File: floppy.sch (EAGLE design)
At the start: 20 parts, among them IC1 ATTINY13-20SU, Q1 S9018

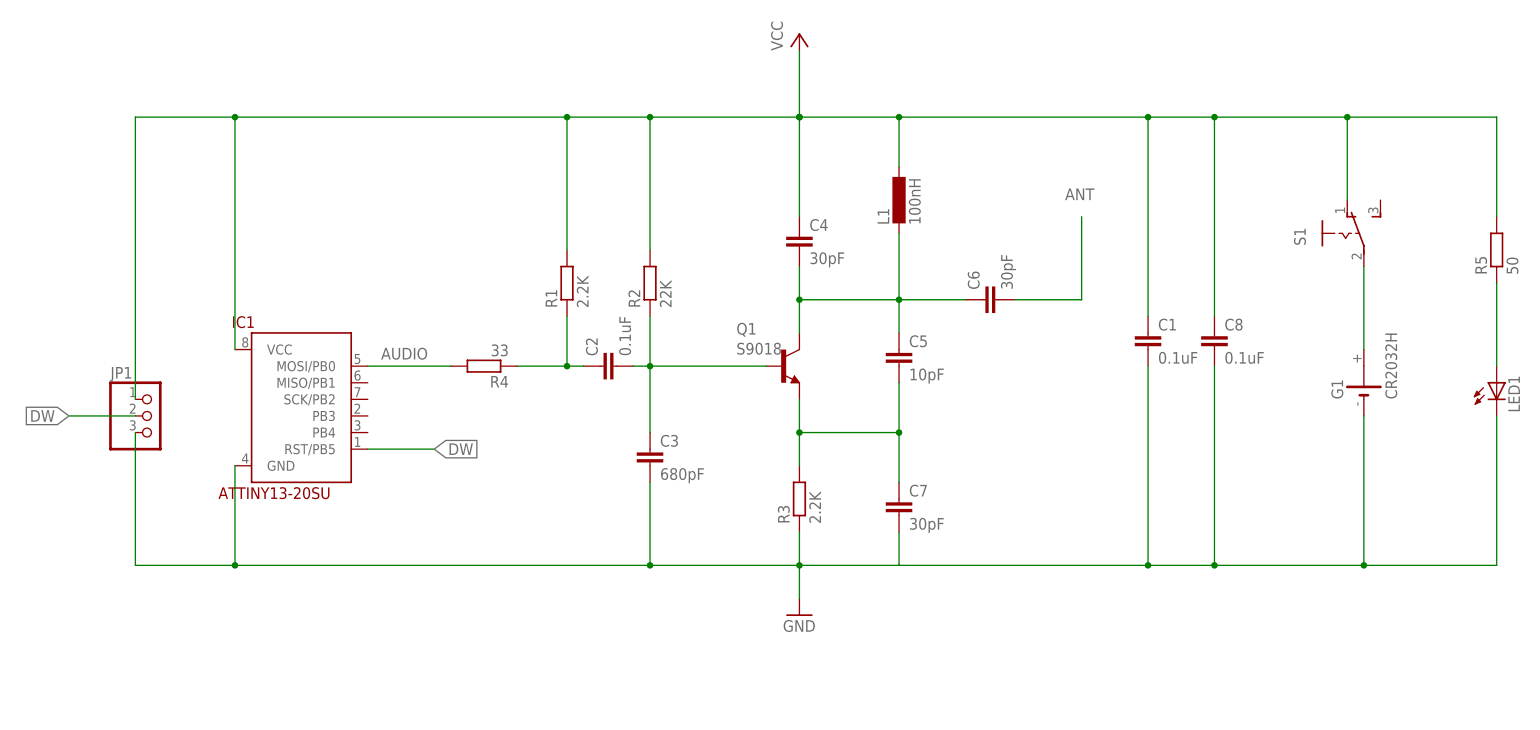
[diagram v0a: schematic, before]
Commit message: Made layout much nicer LED now driven directly from AVR TODO: * check that LED can be driven driectly from AVR * pirate flag and nicer "illegal radio transmitter" text * adjust FM frequency text * check that design works in general
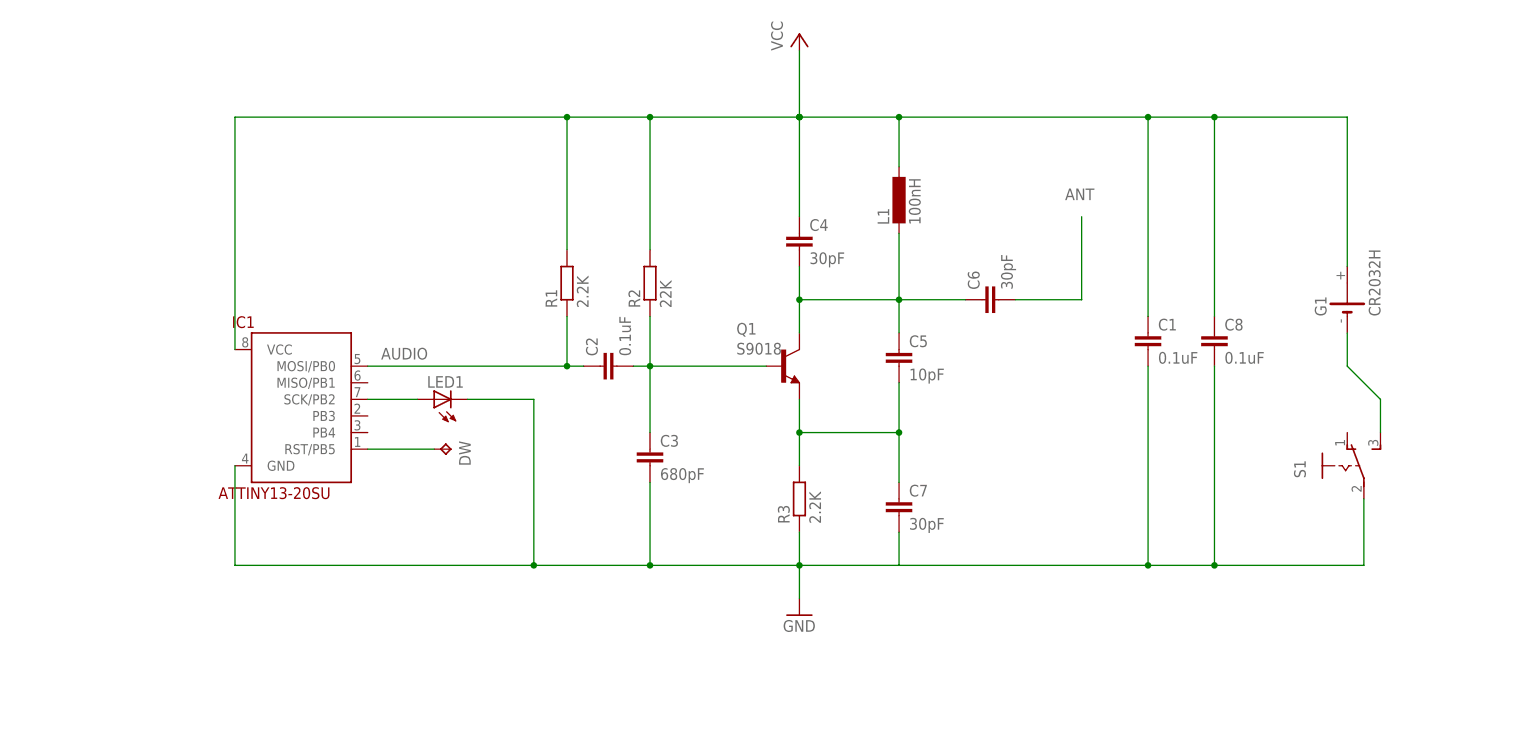
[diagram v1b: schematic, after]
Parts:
- removed JP1: (no value), pinhead:PINHD-1X3
- removed R4: 33, rcl:R-EU_0207/7
- removed R5: 50, rcl:R-EU_0207/7
- added DW: TPB1,27, testpad:TPB1,27
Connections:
- removed net N$9: LED1.A, R5.1
- net AUDIO: now also C2.1, R1.1; no longer R4.2
- net DW: now also DW.TP; no longer JP1.2
- net GND: now also S1.P; no longer G1.-, JP1.3
- net N$3: now also G1.-, S1.S; no longer G1.+, S1.P
- net N$5: now also IC1.SCK/PB2, LED1.A; no longer C2.1, R1.1, R4.1
- net VCC: now also G1.+; no longer JP1.1, R5.2, S1.O
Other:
- moved on the sheet: G1, LED1, S1
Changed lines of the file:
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@@
 <part name="R2" library="rcl" deviceset="R-EU_" device="0207/7" value="22K"/>
 <part name="R3" library="rcl" deviceset="R-EU_" device="0207/7" value="2.2K"/>
-<part name="R4" library="rcl" deviceset="R-EU_" device="0207/7" value="33"/>
 <part name="C1" library="rcl" deviceset="C-EU" device="025-025X050" value="0.1uF"/>
 <part name="C2" library="rcl" deviceset="C-EU" device="025-025X050" value="0.1uF"/>
@@
 <part name="P+1" library="supply1" deviceset="VCC" device=""/>
 <part name="GND1" library="supply1" deviceset="GND" device=""/>
-<part name="R5" library="rcl" deviceset="R-EU_" device="0207/7" value="50"/>
 <part name="LED1" library="led" deviceset="LED" device="5MM"/>
 <part name="IC1" library="attiny13" deviceset="ATTINY13-20*" device="SU"/>
-<part name="JP1" library="pinhead" deviceset="PINHD-1X3" device=""/>
+<part name="DW" library="testpad" deviceset="TP" device="B1,27"/>
 </parts>
 <sheets>
@@
 <instance part="R2" gate="G$1" x="58.42" y="81.28" rot="R90"/>
 <instance part="R3" gate="G$1" x="81.28" y="48.26" rot="R90"/>
-<instance part="R4" gate="G$1" x="33.02" y="68.58" rot="R180"/>
 <instance part="C1" gate="G$1" x="134.62" y="73.66"/>
 <instance part="C2" gate="G$1" x="50.8" y="68.58" rot="R90"/>
@@
 </instance>
 <instance part="L1" gate="G$1" x="96.52" y="93.98"/>
-<instance part="S1" gate="1" x="165.1" y="88.9"/>
-<instance part="G1" gate="1" x="167.64" y="66.04" rot="R90"/>
+<instance part="S1" gate="1" x="165.1" y="53.34"/>
+<instance part="G1" gate="1" x="165.1" y="78.74" rot="R90"/>
 <instance part="P+1" gate="VCC" x="81.28" y="119.38"/>
 <instance part="GND1" gate="1" x="81.28" y="30.48"/>
-<instance part="R5" gate="G$1" x="187.96" y="86.36" rot="R90"/>
-<instance part="LED1" gate="G$1" x="187.96" y="66.04"/>
+<instance part="LED1" gate="G$1" x="25.4" y="63.5" rot="R90"/>
 <instance part="IC1" gate="G$1" x="5.08" y="63.5"/>
-<instance part="JP1" gate="A" x="-17.78" y="60.96"/>
+<instance part="DW" gate="G$1" x="27.94" y="55.88" rot="R270"/>
 </instances>
 <busses>
 </busses>
 <nets>
-<net name="N$3" class="0">
-<segment>
-<pinref part="S1" gate="1" pin="P"/>
-<pinref part="G1" gate="1" pin="+"/>
-<wire x1="167.64" y1="71.12" x2="167.64" y2="83.82" width="0.1524" layer="91"/>
-</segment>
-</net>
 <net name="GND" class="0">
 <segment>
@@
 <pinref part="GND1" gate="1" pin="GND"/>
 <wire x1="81.28" y1="33.02" x2="81.28" y2="38.1" width="0.1524" layer="91"/>
-<pinref part="G1" gate="1" pin="-"/>
 <wire x1="81.28" y1="38.1" x2="81.28" y2="43.18" width="0.1524" layer="91"/>
 <wire x1="58.42" y1="38.1" x2="81.28" y2="38.1" width="0.1524" layer="91"/>
@@
 <wire x1="134.62" y1="38.1" x2="144.78" y2="38.1" width="0.1524" layer="91"/>
 <wire x1="144.78" y1="38.1" x2="167.64" y2="38.1" width="0.1524" layer="91"/>
-<wire x1="167.64" y1="38.1" x2="167.64" y2="60.96" width="0.1524" layer="91"/>
 <pinref part="C3" gate="G$1" pin="2"/>
 <wire x1="58.42" y1="50.8" x2="58.42" y2="38.1" width="0.1524" layer="91"/>
@@
 <wire x1="144.78" y1="68.58" x2="144.78" y2="38.1" width="0.1524" layer="91"/>
 <junction x="144.78" y="38.1"/>
-<wire x1="167.64" y1="38.1" x2="187.96" y2="38.1" width="0.1524" layer="91"/>
-<wire x1="187.96" y1="38.1" x2="187.96" y2="60.96" width="0.1524" layer="91"/>
-<pinref part="LED1" gate="G$1" pin="C"/>
-<junction x="167.64" y="38.1"/>
 <pinref part="C1" gate="G$1" pin="2"/>
 <wire x1="134.62" y1="68.58" x2="134.62" y2="38.1" width="0.1524" layer="91"/>
 <junction x="134.62" y="38.1"/>
-<wire x1="58.42" y1="38.1" x2="-5.08" y2="38.1" width="0.1524" layer="91"/>
+<wire x1="58.42" y1="38.1" x2="40.64" y2="38.1" width="0.1524" layer="91"/>
 <pinref part="IC1" gate="G$1" pin="GND"/>
-<wire x1="-5.08" y1="38.1" x2="-20.32" y2="38.1" width="0.1524" layer="91"/>
+<wire x1="40.64" y1="38.1" x2="-5.08" y2="38.1" width="0.1524" layer="91"/>
 <wire x1="-5.08" y1="53.34" x2="-5.08" y2="38.1" width="0.1524" layer="91"/>
-<junction x="-5.08" y="38.1"/>
-<pinref part="JP1" gate="A" pin="3"/>
-<wire x1="-20.32" y1="38.1" x2="-20.32" y2="58.42" width="0.1524" layer="91"/>
 <junction x="58.42" y="38.1"/>
 <junction x="81.28" y="38.1"/>
+<pinref part="LED1" gate="G$1" pin="C"/>
+<wire x1="30.48" y1="63.5" x2="40.64" y2="63.5" width="0.1524" layer="91"/>
+<wire x1="40.64" y1="63.5" x2="40.64" y2="38.1" width="0.1524" layer="91"/>
+<junction x="40.64" y="38.1"/>
+<pinref part="S1" gate="1" pin="P"/>
+<wire x1="167.64" y1="38.1" x2="167.64" y2="48.26" width="0.1524" layer="91"/>
 </segment>
 </net>
 <net name="VCC" class="0">
 <segment>
-<pinref part="S1" gate="1" pin="O"/>
-<wire x1="165.1" y1="93.98" x2="165.1" y2="106.68" width="0.1524" layer="91"/>
 <wire x1="165.1" y1="106.68" x2="144.78" y2="106.68" width="0.1524" layer="91"/>
 <wire x1="144.78" y1="106.68" x2="134.62" y2="106.68" width="0.1524" layer="91"/>
@@
 <wire x1="144.78" y1="76.2" x2="144.78" y2="106.68" width="0.1524" layer="91"/>
 <junction x="144.78" y="106.68"/>
-<wire x1="165.1" y1="106.68" x2="187.96" y2="106.68" width="0.1524" layer="91"/>
-<wire x1="187.96" y1="106.68" x2="187.96" y2="91.44" width="0.1524" layer="91"/>
-<pinref part="R5" gate="G$1" pin="2"/>
-<junction x="165.1" y="106.68"/>
 <pinref part="C1" gate="G$1" pin="1"/>
 <wire x1="134.62" y1="106.68" x2="134.62" y2="76.2" width="0.1524" layer="91"/>
@@
 <wire x1="45.72" y1="106.68" x2="-5.08" y2="106.68" width="0.1524" layer="91"/>
 <pinref part="IC1" gate="G$1" pin="VCC"/>
-<wire x1="-5.08" y1="106.68" x2="-20.32" y2="106.68" width="0.1524" layer="91"/>
 <wire x1="-5.08" y1="71.12" x2="-5.08" y2="106.68" width="0.1524" layer="91"/>
-<pinref part="JP1" gate="A" pin="1"/>
-<wire x1="-20.32" y1="63.5" x2="-20.32" y2="106.68" width="0.1524" layer="91"/>
-<junction x="-5.08" y="106.68"/>
 <junction x="45.72" y="106.68"/>
+<pinref part="G1" gate="1" pin="+"/>
+<wire x1="165.1" y1="83.82" x2="165.1" y2="106.68" width="0.1524" layer="91"/>
 </segment>
 </net>
@@
 </segment>
 </net>
-<net name="N$5" class="0">
-<segment>
+<net name="ANT" class="0">
+<segment>
+<pinref part="C6" gate="G$1" pin="2"/>
+<wire x1="114.3" y1="78.74" x2="124.46" y2="78.74" width="0.1524" layer="91"/>
+<wire x1="124.46" y1="78.74" x2="124.46" y2="91.44" width="0.1524" layer="91"/>
+<label x="121.92" y="93.98" size="1.778" layer="95"/>
+</segment>
+</net>
+<net name="AUDIO" class="0">
+<segment>
+<label x="17.272" y="69.596" size="1.778" layer="95"/>
+<pinref part="IC1" gate="G$1" pin="MOSI/PB0"/>
+<wire x1="45.72" y1="68.58" x2="15.24" y2="68.58" width="0.1524" layer="91"/>
 <pinref part="R1" gate="G$1" pin="1"/>
 <pinref part="C2" gate="G$1" pin="1"/>
 <wire x1="45.72" y1="76.2" x2="45.72" y2="68.58" width="0.1524" layer="91"/>
 <wire x1="45.72" y1="68.58" x2="48.26" y2="68.58" width="0.1524" layer="91"/>
-<pinref part="R4" gate="G$1" pin="1"/>
-<wire x1="45.72" y1="68.58" x2="38.1" y2="68.58" width="0.1524" layer="91"/>
 <junction x="45.72" y="68.58"/>
-</segment>
-</net>
-<net name="ANT" class="0">
-<segment>
-<pinref part="C6" gate="G$1" pin="2"/>
-<wire x1="114.3" y1="78.74" x2="124.46" y2="78.74" width="0.1524" layer="91"/>
-<wire x1="124.46" y1="78.74" x2="124.46" y2="91.44" width="0.1524" layer="91"/>
-<label x="121.92" y="93.98" size="1.778" layer="95"/>
-</segment>
-</net>
-<net name="N$9" class="0">
-<segment>
-<pinref part="R5" gate="G$1" pin="1"/>
-<pinref part="LED1" gate="G$1" pin="A"/>
-<wire x1="187.96" y1="68.58" x2="187.96" y2="81.28" width="0.1524" layer="91"/>
-</segment>
-</net>
-<net name="AUDIO" class="0">
-<segment>
-<pinref part="R4" gate="G$1" pin="2"/>
-<label x="17.272" y="69.596" size="1.778" layer="95"/>
-<pinref part="IC1" gate="G$1" pin="MOSI/PB0"/>
-<wire x1="27.94" y1="68.58" x2="15.24" y2="68.58" width="0.1524" layer="91"/>
 </segment>
 </net>
@@
 <pinref part="IC1" gate="G$1" pin="RST/PB5"/>
 <wire x1="25.4" y1="55.88" x2="15.24" y2="55.88" width="0.1524" layer="91"/>
-<label x="25.4" y="55.88" size="1.778" layer="95" xref="yes"/>
-</segment>
-<segment>
-<pinref part="JP1" gate="A" pin="2"/>
-<wire x1="-20.32" y1="60.96" x2="-30.48" y2="60.96" width="0.1524" layer="91"/>
-<label x="-30.48" y="60.96" size="1.778" layer="95" rot="R180" xref="yes"/>
-</segment>
-</net>
+<pinref part="DW" gate="G$1" pin="TP"/>
+</segment>
+</net>
+<net name="N$5" class="0">
+<segment>
+<pinref part="IC1" gate="G$1" pin="SCK/PB2"/>
+<pinref part="LED1" gate="G$1" pin="A"/>
+<wire x1="15.24" y1="63.5" x2="22.86" y2="63.5" width="0.1524" layer="91"/>
+</segment>
+</net>
+<net name="N$3" class="0">
+<segment>
+<pinref part="S1" gate="1" pin="S"/>
+<wire x1="170.18" y1="58.42" x2="170.18" y2="63.5" width="0.1524" layer="91"/>
+<wire x1="170.18" y1="63.5" x2="165.1" y2="68.58" width="0.1524" layer="91"/>
+<pinref part="G1" gate="1" pin="-"/>
+<wire x1="165.1" y1="68.58" x2="165.1" y2="73.66" width="0.1524" layer="91"/>
+</segment>
+</net>

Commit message: Fixed battery holder footprint Added "Illegal radio transmitter"
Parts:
- G1: value CR2032H -> BK-913; device battery:CR2032H -> local:BK-913
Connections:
- net N$3: now also G1.V-; no longer G1.-
- net VCC: now also G1.V+; no longer G1.+
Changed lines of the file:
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@@
 <part name="L1" library="rcl" deviceset="L-EU" device="0207/7" value="100nH"/>
 <part name="S1" library="switch" deviceset="255SB" device=""/>
-<part name="G1" library="battery" deviceset="CR2032H" device=""/>
+<part name="G1" library="local" deviceset="BK-913" device=""/>
 <part name="P+1" library="supply1" deviceset="VCC" device=""/>
 <part name="GND1" library="supply1" deviceset="GND" device=""/>
@@
 <instance part="L1" gate="G$1" x="96.52" y="93.98"/>
 <instance part="S1" gate="1" x="165.1" y="53.34"/>
-<instance part="G1" gate="1" x="165.1" y="78.74" rot="R90"/>
+<instance part="G1" gate="G$1" x="165.1" y="78.74" rot="R90"/>
 <instance part="P+1" gate="VCC" x="81.28" y="119.38"/>
 <instance part="GND1" gate="1" x="81.28" y="30.48"/>
@@
 <wire x1="-5.08" y1="71.12" x2="-5.08" y2="106.68" width="0.1524" layer="91"/>
 <junction x="45.72" y="106.68"/>
-<pinref part="G1" gate="1" pin="+"/>
+<pinref part="G1" gate="G$1" pin="V+"/>
 <wire x1="165.1" y1="83.82" x2="165.1" y2="106.68" width="0.1524" layer="91"/>
 </segment>
@@
 <wire x1="170.18" y1="58.42" x2="170.18" y2="63.5" width="0.1524" layer="91"/>
 <wire x1="170.18" y1="63.5" x2="165.1" y2="68.58" width="0.1524" layer="91"/>
-<pinref part="G1" gate="1" pin="-"/>
+<pinref part="G1" gate="G$1" pin="V-"/>
 <wire x1="165.1" y1="68.58" x2="165.1" y2="73.66" width="0.1524" layer="91"/>
 </segment>

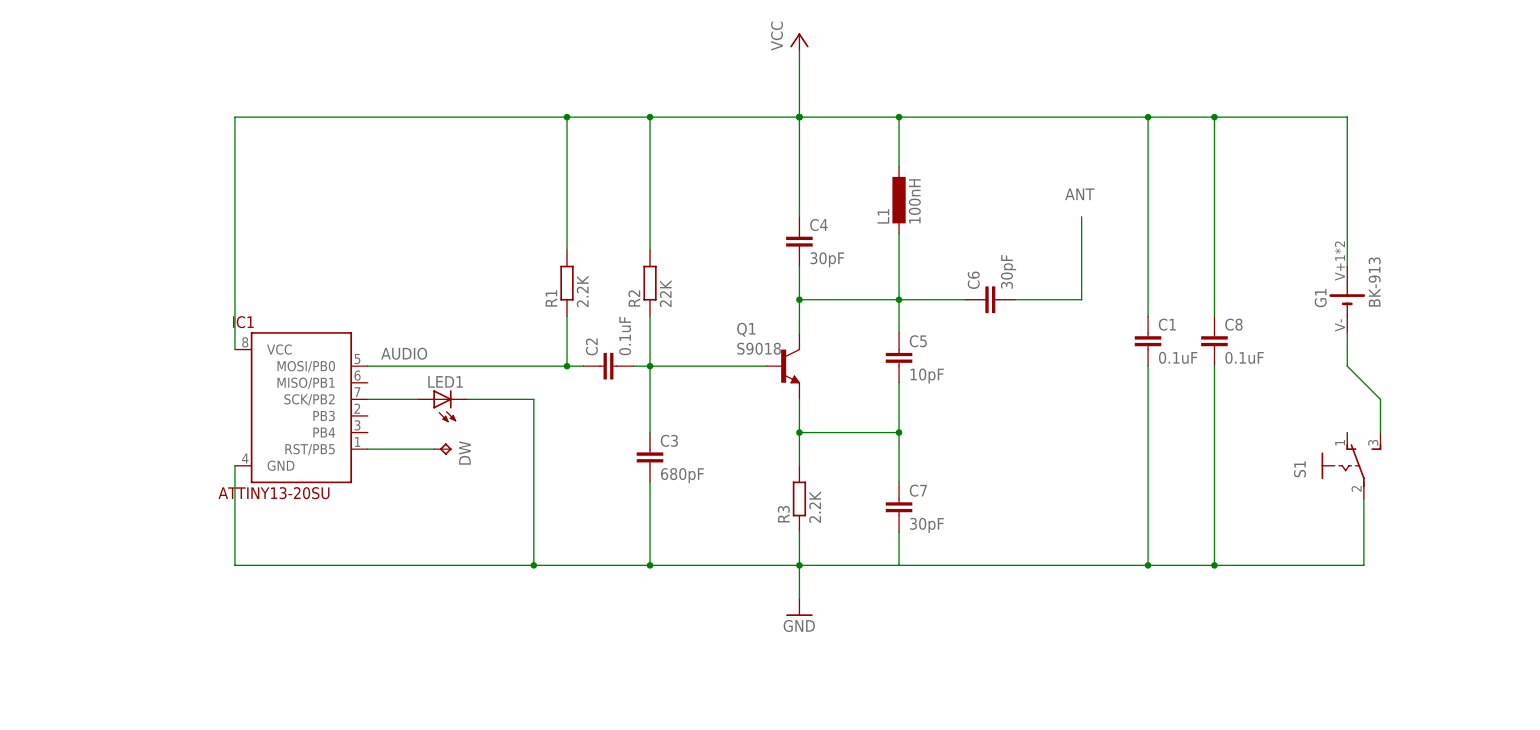
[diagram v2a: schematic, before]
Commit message: New circuit that has been tested to work up front
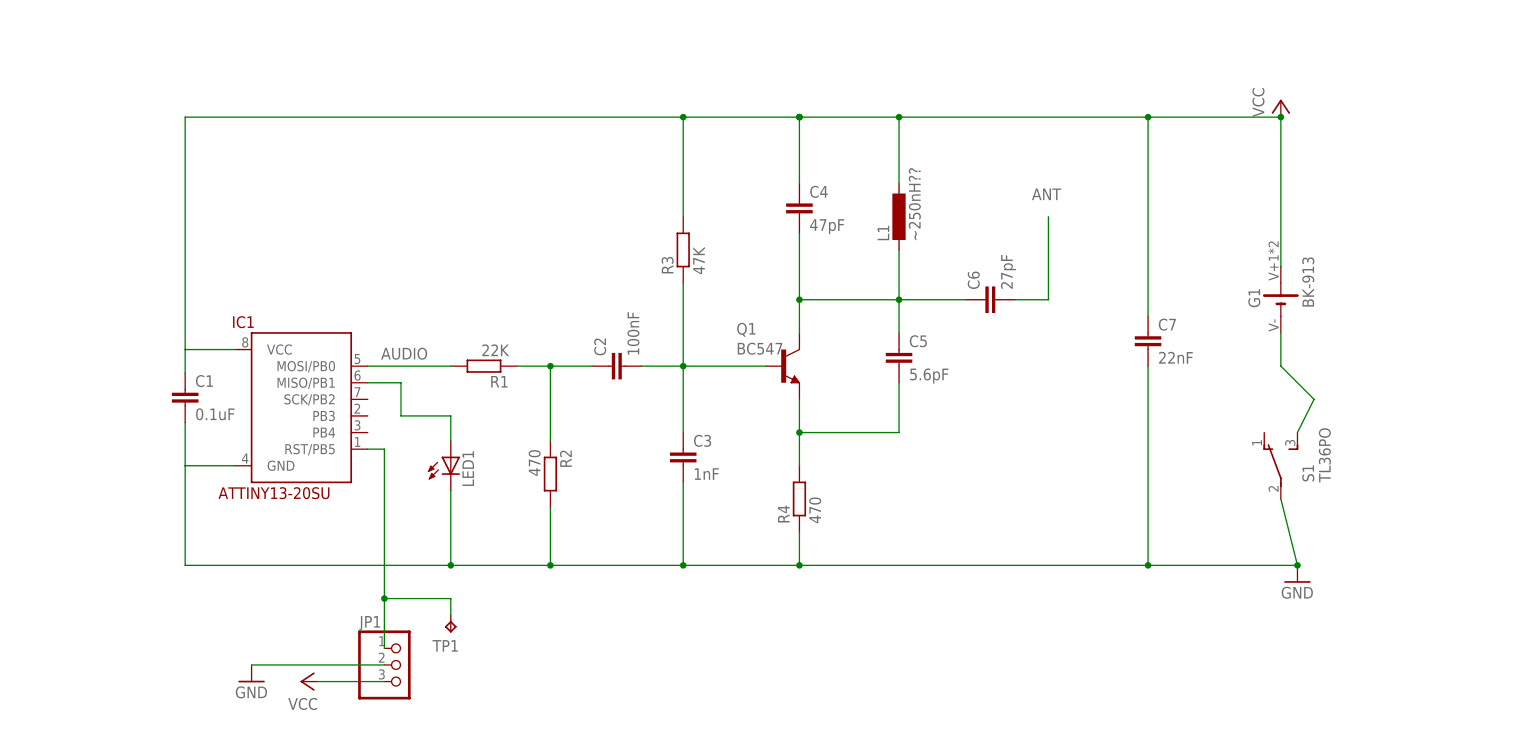
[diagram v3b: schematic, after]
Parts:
- removed C8: 0.1uF, rcl:C-EU025-025X050
- removed DW: TPB1,27, testpad:TPB1,27
- added JP1: (no value), pinhead:PINHD-1X3
- added R4: 470, rcl:R-EU_0207/7
- added TP1: TPB1,27, testpad:TPB1,27
- C2: value 0.1uF -> 100nF
- C3: value 680pF -> 1nF
- C4: value 30pF -> 47pF
- C5: value 10pF -> 5.6pF
- C6: value 30pF -> 27pF
- C7: value 30pF -> 22nF
- L1: value 100nH -> ~250nH??
- Q1: value S9018 -> BC547; device transistor-npn:2N3565 -> transistor-npn:BC547
- R1: value 2.2K -> 22K
- R2: value 22K -> 470
- R3: value 2.2K -> 47K
- S1: value (none) -> TL36PO; device switch:255SB -> switch:TL36PO
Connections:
- new net N$4: IC1.MOSI/PB0, R1.2
- net AUDIO: now also R2.1; no longer IC1.MOSI/PB0
- net DW: now also JP1.1, TP1.TP; no longer DW.TP
- net GND: now also JP1.2, R2.2, R4.1; no longer C8.2, R3.1
- net N$5: now also IC1.MISO/PB1; no longer IC1.SCK/PB2
- net N$7: now also R4.2; no longer C7.1, R3.2
- net N$8: now also R3.1; no longer R2.1
- net VCC: now also C7.1, JP1.3, R3.2; no longer C8.1, R1.2, R2.2
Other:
- moved on the sheet: C1, C2, C3, C4, C7, G1, L1, LED1, R1, R2, R3

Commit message: Changed to 96HZ, added circle on back
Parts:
- L1: value ~250nH?? -> (none)
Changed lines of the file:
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@@
 <?xml version="1.0" encoding="utf-8"?>
 <!DOCTYPE eagle SYSTEM "eagle.dtd">
-<eagle version="7.7.0">
+<eagle version="8.3.1">
 <drawing>
 <settings>
 <setting alwaysvectorfont="no"/>
+<setting keepoldvectorfont="yes"/>
 <setting verticaltext="up"/>
 </settings>
-<grid distance="0.1" unitdist="inch" unit="inch" style="lines" multiple="1" display="no" altdistance="0.05" altunitdist="inch" altunit="inch"/>
+<grid distance="0.1" unitdist="inch" unit="inch" style="lines" multiple="1" display="no" altdistance="0.01" altunitdist="inch" altunit="inch"/>
 <layers>
 <layer number="1" name="Top" color="4" fill="1" visible="no" active="no"/>
@@
 <part name="C7" library="rcl" deviceset="C-EU" device="025-025X050" value="22nF"/>
 <part name="Q1" library="transistor-npn" deviceset="BC547*" device="" value="BC547"/>
-<part name="L1" library="rcl" deviceset="L-EU" device="0207/7" value="~250nH??"/>
+<part name="L1" library="rcl" deviceset="L-EU" device="0207/7"/>
 <part name="S1" library="switch" deviceset="TL36PO" device=""/>
 <part name="G1" library="local" deviceset="BK-913" device=""/>
